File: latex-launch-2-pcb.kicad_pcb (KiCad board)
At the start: 4 copper layers, 9 parts, among them J1 Conn_RockBLOCK, J2 Switch_RockBLOCK, J3 Conn_FeatherWeight, J4 Conn_LightAPRS, J5 Conn_MicroSD

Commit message: idk
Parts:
- added H1: MountingHole, MountingHole:MountingHole_3.2mm_M3_DIN965_Pad, F.Cu at (114.6, 73.9)
- added H2: MountingHole, MountingHole:MountingHole_3.2mm_M3_DIN965_Pad, F.Cu at (114.6, 129.5)
- added H3: MountingHole, MountingHole:MountingHole_3.2mm_M3_DIN965_Pad, F.Cu at (186.7, 129.5)
- added H4: MountingHole, MountingHole:MountingHole_3.2mm_M3_DIN965_Pad, F.Cu at (186.7, 73.9)
- added J6: Conn_GY-512_MPU6050, Module:GY-521 MPU6050, F.Cu at (152.7, 91.4)
- moved J2 112.7 mm to (183.9, 122.7), turned to 180 degrees
- moved J1 111.1 mm to (186.6, 109.8), turned to 90 degrees
- moved J3 107.7 mm to (186.3, 86.9), turned to 90 degrees
- moved R2 100.7 mm to (169.2, 106.2), turned to 90 degrees
- moved R1 94.2 mm to (174.2, 96.0), turned to -90 degrees
- moved A1 83.6 mm to (133.6, 129.4), turned to 90 degrees
- moved J4 70.6 mm to (117.2, 115.3)
- moved C1 43.4 mm to (148.8, 105.7), turned to 180 degrees
- moved J5 5.93 mm to (123.7, 91.2), turned to 90 degrees
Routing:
- net +BATT: track 0.00 -> 96.5 mm, vias 0 -> 2
- net /I2C_SDA: track 0.00 -> 90.7 mm, vias 0 -> 3
- net /I2C_SCL: track 0.00 -> 82.8 mm, vias 0 -> 3
- net +3V3: track 0.00 -> 73.4 mm, vias 0 -> 2
- net /CS_SDCard: track 0.00 -> 68.3 mm, vias 0 -> 2
- net /SPI_MISO: track 0.00 -> 60.3 mm, vias 0 -> 1
- net /SPI_MOSI: track 0.00 -> 59.3 mm, vias 0 -> 3
- net /SPI_SCK: track 0.00 -> 53.7 mm, vias 0 -> 1
- net /Tx: track 0.00 -> 21.1 mm
- net /Rx: track 0.00 -> 21.1 mm
- net /Tx_RockBLOCK: track 0.00 -> 15.3 mm
- net /Rx_RockBLOCK: track 0.00 -> 8.97 mm
- added copper zone on F.Cu, net GND
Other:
- board outline added: 82.6 x 66.3 mm

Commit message: better pcb
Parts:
- moved H4 118.2 mm to (68.6, 68.6)
- moved J3 117.8 mm to (70.6, 108.7), turned to -90 degrees
- moved J1 106.5 mm to (81.8, 128.2)
- moved J2 98.2 mm to (87.1, 105.9), turned to 0 degrees
- moved H3 80.2 mm to (134.6, 68.6)
- moved R1 79.5 mm to (95.5, 85.1), turned to 0 degrees
- moved H1 76.3 mm to (68.3, 134.6)
- moved R2 69.0 mm to (105.7, 79.2), turned to 180 degrees
- moved A1 52.1 mm to (110.9, 82.5), turned to 0 degrees
- moved J6 52.1 mm to (101.6, 101.6), turned to 0 degrees
- moved C1 49.0 mm to (101.1, 116.8), turned to 0 degrees
- moved J4 47.4 mm to (70.5, 123.4)
- moved J5 46.6 mm to (77.2, 88.6)
- moved H2 20.7 mm to (134.6, 134.6)
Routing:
- net +3V3: track 73.4 -> 39.8 mm, vias 2 -> 0
- net /I2C_SCL: track 82.8 -> 111.7 mm, vias 3 -> 1
- net /SPI_MISO: track 60.3 -> 34.1 mm, vias 1 -> 0
- net /SPI_MOSI: track 59.3 -> 34.3 mm, vias 3 -> 0
- net /I2C_SDA: track 90.7 -> 105.4 mm, vias 3 -> 1
- net +BATT: track 96.5 -> 109.7 mm, vias 2 -> 0
- net /SPI_SCK: track 53.7 -> 42.0 mm, vias 1 -> 0
- net /CS_SDCard: track 68.3 -> 57.3 mm, vias 2 -> 0
- net /Rx_RockBLOCK: track 8.97 -> 19.4 mm
- net /Tx: track 21.1 -> 30.5 mm
- net /Rx: track 21.1 -> 26.7 mm
- net /Tx_RockBLOCK: track 15.3 -> 12.3 mm
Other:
- board size 82.6 x 66.3 mm -> 76.2 x 76.2 mm

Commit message: PCB version 2
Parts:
- removed H1, H2, H3, H4: MountingHole, MountingHole:MountingHole_3.2mm_M3_DIN965_Pad
- added J7: Conn_MicroSD, Latex Launch 2 Footprints:Adafruit_MicroSD_Breakout, F.Cu at (228.6, 113.0)
- added J8: Conn_HTU21DF, Latex Launch 2 Footprints:Adafruit_HTU21DF_Breakout, F.Cu at (174.1, 117.5)
- added R3: R_shunt, Connector_PinHeader_2.54mm:PinHeader_1x02_P2.54mm_Vertical, F.Cu at (201.9, 67.3)
- added R4: R_shunt, Connector_PinHeader_2.54mm:PinHeader_1x02_P2.54mm_Vertical, F.Cu at (207.3, 67.3)
- added U1: ~, Latex Launch 2 Footprints:Adafruit_RFM96W_LoRa_Breakout, F.Cu at (200.6, 110.7)
- A1: value Adafruit_Feather_M0_RFM9x_LoRa_Radio -> Adafruit_Feather_M0_Express; footprint Module:Adafruit_Feather_M0_RFM -> Module:Adafruit_Feather_M0_RFM_WithMountingHoles
- C1: value C0.1u -> C; footprint Capacitor_THT:C_Rect_L7.0mm_W2.5mm_P5.00mm -> Capacitor_THT:C_Rect_L4.6mm_W2.0mm_P2.50mm_MKS02_FKP02
- J1: value Conn_RockBLOCK -> Conn_GPS; footprint Connector_Molex:Molex_PicoBlade_53047-1010_1x10_P1.25mm_Vertical -> Latex Launch 2 Footprints:Adafruit_GPS_Breakout
- J2: value Switch_RockBLOCK -> Conn_LightAPRS-W_2.0; footprint Connector_PinSocket_2.54mm:PinSocket_2x03_P2.54mm_Vertical -> Connector_JST:JST_PH_S4B-PH-SM4-TB_1x04-1MP_P2.00mm_Horizontal
- J4: value Conn_LightAPRS -> Conn_RockBLOCK; footprint Connector_JST:JST_PH_S4B-PH-SM4-TB_1x04-1MP_P2.00mm_Horizontal -> Connector_Molex:Molex_PicoBlade_53047-1010_1x10_P1.25mm_Vertical
- J5: value Conn_MicroSD -> Conn_GY512_MPU6050; footprint Module:Adafruit_MicroSD_Breakout -> Latex Launch 2 Footprints:GY-521 MPU6050
- J6: value Conn_GY-512_MPU6050 -> Conn_BMP280; footprint Module:GY-521 MPU6050 -> Latex Launch 2 Footprints:Adafruit_BMP280_Breakout
- R1, R2: value R10k -> 10k
- moved J4 174.3 mm to (230.4, 54.0), turned to 90 degrees
- moved J1 150.7 mm to (224.8, 80.5), turned to 180 degrees
- moved J5 126.1 mm to (203.2, 82.5), turned to 0 degrees
- moved J3 104.7 mm to (172.2, 83.6)
- moved R1 96.1 mm to (190.5, 70.9), turned to 180 degrees
- moved J2 92.3 mm to (172.2, 70.1), turned to -90 degrees
- moved C1 88.2 mm to (168.7, 60.2)
- moved R2 86.1 mm to (190.5, 64.5)
- moved J6 75.0 mm to (176.5, 99.3), turned to 90 degrees
- moved A1 72.9 mm to (180.3, 60.6), turned to 90 degrees
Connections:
- A1 pad 14: /Rx -> Net-(A1-RX/D0)
- A1 pad 15: /Tx -> Net-(A1-TX/D1)
- A1 pad 19: /CS_SDCard -> /CS_SD
- A1 pad 20: unconnected-(A1-D6-Pad20) -> /EN_GPS
- A1 pad 21: unconnected-(A1-D9-Pad21) -> /EN_RockBLOCK
- A1 pad 22: unconnected-(A1-D10-Pad22) -> /CS_RFM96W
- A1 pad 23: unconnected-(A1-D11-Pad23) -> /CS_BMP280
- A1 pad 26: +BATT -> unconnected-(A1-USB-Pad26)
- A1 pad 28: unconnected-(A1-VBAT-Pad28) -> +BATT
- A1 pad 29: unconnected-(A1-ANT-Pad29) -> (no net)
- A1 pad 30: unconnected-(A1-DIO5-Pad30) -> (no net)
- A1 pad 31: unconnected-(A1-DIO3-Pad31) -> (no net)
- A1 pad 32: unconnected-(A1-DIO2-Pad32) -> (no net)
- J1 pad 1: /Rx_RockBLOCK -> unconnected-(J1-Pin_1-Pad1)
- J1 pad 2: unconnected-(J1-Pin_2-Pad2) -> /EN_GPS
- J1 pad 5: unconnected-(J1-Pin_5-Pad5) -> /Rx_iso
- J1 pad 6: /Tx_RockBLOCK -> /Tx_iso
- J1 pad 7: unconnected-(J1-Pin_7-Pad7) -> GND
- J1 pad 8: +BATT -> +3V3
- J2 pad 1: unconnected-(J2-Pin_1-Pad1) -> /I2C_SCL
- J2 pad 2: unconnected-(J2-Pin_2-Pad2) -> /I2C_SDA
- J2 pad 3: /Rx -> +BATT
- J2 pad 4: /Tx -> GND
- J3 pad 1: +BATT -> +3V3
- J4 pad 1: GND -> /Rx_iso
- J4 pad 2: +BATT -> unconnected-(J4-Pin_2-Pad2)
- J4 pad 3: /I2C_SCL -> unconnected-(J4-Pin_3-Pad3)
- J4 pad 4: /I2C_SDA -> unconnected-(J4-Pin_4-Pad4)
- J5 pad 3: /SPI_SCK -> /I2C_SCL
- J5 pad 4: /SPI_MISO -> /I2C_SDA
- J5 pad 5: /SPI_MOSI -> unconnected-(J5-Pin_5-Pad5)
- J5 pad 6: /CS_SDCard -> unconnected-(J5-Pin_6-Pad6)
- J6 pad 1: +BATT -> +3V3
- J6 pad 2: GND -> unconnected-(J6-Pin_2-Pad2)
- J6 pad 3: /I2C_SCL -> GND
- J6 pad 4: /I2C_SDA -> /SPI_SCK
- J6 pad 5: unconnected-(J6-Pin_5-Pad5) -> /SPI_MISO
- J6 pad 6: unconnected-(J6-Pin_6-Pad6) -> /SPI_MOSI
- J6 pad 7: unconnected-(J6-Pin_7-Pad7) -> /CS_BMP280
- R2 pad 1: /I2C_SCL -> +3V3
- R2 pad 2: +3V3 -> /I2C_SCL
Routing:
- net +3V3: track 39.8 -> 148.8 mm, vias 0 -> 1
- net /CS_SD: track 0.00 -> 78.9 mm
- net /CS_RFM96W: track 0.00 -> 64.7 mm
- net /CS_BMP280: track 0.00 -> 59.6 mm
- net /SPI_MOSI: track 34.3 -> 92.1 mm, vias 0 -> 2
- net /CS_SDCard: track 57.3 -> 0.00 mm
- net /SPI_MISO: track 34.1 -> 89.1 mm, vias 0 -> 2
- net /SPI_SCK: track 42.0 -> 94.0 mm
- net /EN_GPS: track 0.00 -> 42.9 mm
- net /Rx_iso: track 0.00 -> 38.6 mm
- net /Tx_iso: track 0.00 -> 37.1 mm
- net /Tx: track 30.5 -> 0.00 mm
- net /EN_RockBLOCK: track 0.00 -> 29.6 mm
- net /Rx: track 26.7 -> 0.00 mm
- net +BATT: track 109.7 -> 86.6 mm
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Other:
- board size 76.2 x 76.2 mm -> 76.2 x 88.9 mm

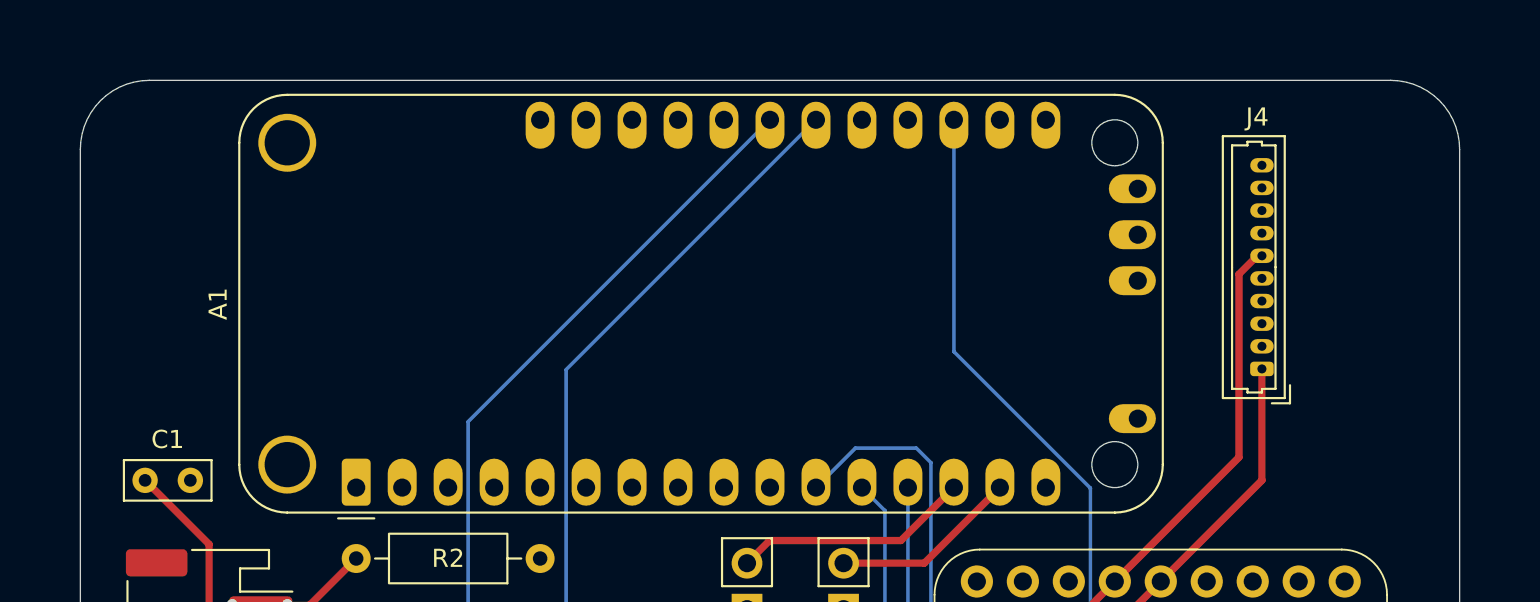
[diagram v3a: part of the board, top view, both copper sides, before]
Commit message: PCB v2 added mounting holes
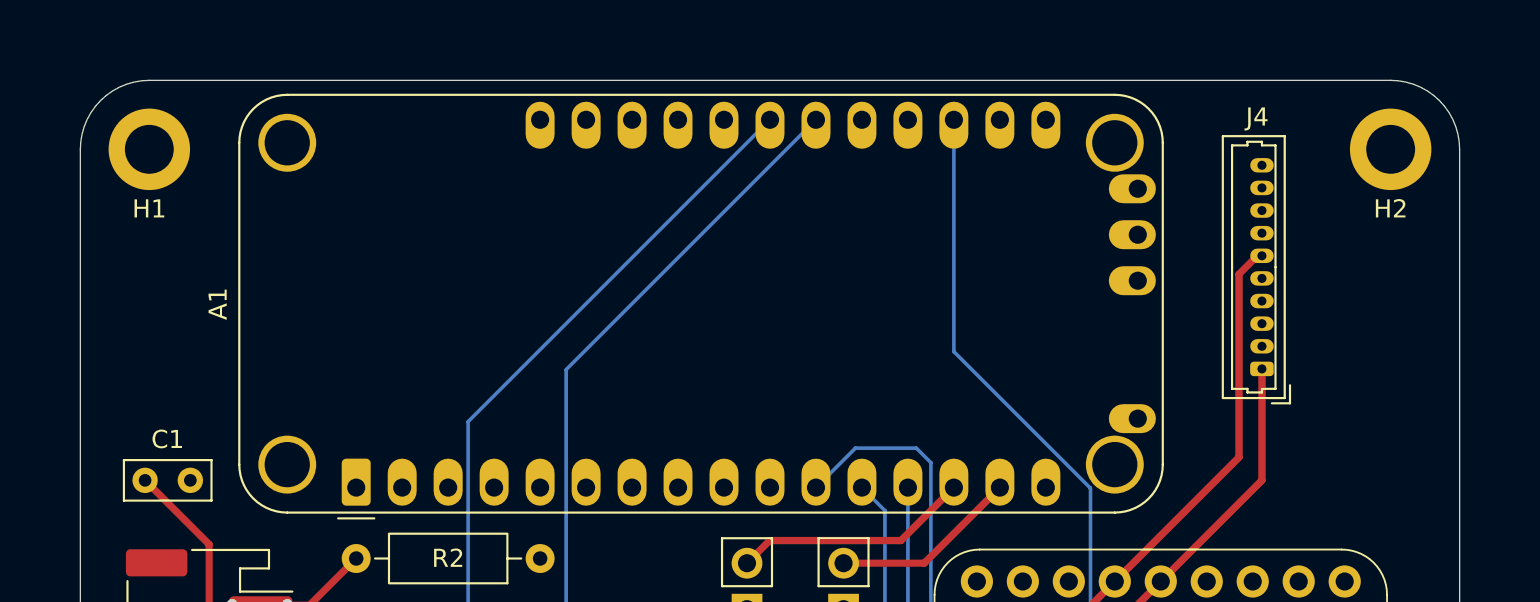
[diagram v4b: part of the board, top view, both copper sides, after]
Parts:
- added H1: MountingHole, MountingHole:MountingHole_2.7mm_M2.5_ISO7380_Pad, F.Cu at (168.9, 41.9)
- added H2: MountingHole, MountingHole:MountingHole_2.7mm_M2.5_ISO7380_Pad, F.Cu at (237.5, 41.9)
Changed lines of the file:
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@@
 		)
+	)
+	(footprint "MountingHole:MountingHole_2.7mm_M2.5_ISO7380_Pad"
+		(layer "F.Cu")
+		(at 168.91 41.91)
+		(descr "Mounting Hole 2.7mm, M2.5, generated by kicad-footprint-generator mountinghole.py")
+		(tags "mountinghole M2.5 ISO7380")
+		(property "Reference" "H1"
+			(at 0 3.302 0)
+			(layer "F.SilkS")
+			(effects
+				(font
+					(size 1 1)
+					(thickness 0.15)
+				)
+			)
+		)
+		(property "Value" "MountingHole"
+			(at 3.302 2.032 90)
+			(layer "F.Fab")
+			(effects
+				(font
+					(size 1 1)
+					(thickness 0.15)
+				)
+			)
+		)
+		(property "Datasheet" "~"
+			(at 0 0 0)
+			(layer "F.Fab")
+			(hide yes)
+			(effects
+				(font
+					(size 1.27 1.27)
+					(thickness 0.15)
+				)
+			)
+		)
+		(property "Description" "Mounting Hole without connection"
+			(at 0 0 0)
+			(layer "F.Fab")
+			(hide yes)
+			(effects
+				(font
+					(size 1.27 1.27)
+					(thickness 0.15)
+				)
+			)
+		)
+		(property ki_fp_filters "MountingHole*")
+		(sheetname "/")
+		(sheetfile "latex-launch-2-pcb.kicad_sch")
+		(attr exclude_from_pos_files exclude_from_bom)
+		(fp_circle
+			(center 0 0)
+			(end 2.25 0)
+			(stroke
+				(width 0.15)
+				(type solid)
+			)
+			(fill no)
+			(layer "Cmts.User")
+		)
+		(fp_circle
+			(center 0 0)
+			(end 2.5 0)
+			(stroke
+				(width 0.05)
+				(type solid)
+			)
+			(fill no)
+			(layer "F.CrtYd")
+		)
+		(fp_text user "${REFERENCE}"
+			(at 0 0 0)
+			(layer "F.Fab")
+			(effects
+				(font
+					(size 1 1)
+					(thickness 0.15)
+				)
+			)
+		)
+		(pad "1" thru_hole circle
+			(at 0 0)
+			(size 4.5 4.5)
+			(drill 2.7)
+			(layers "*.Cu" "*.Mask")
+			(remove_unused_layers no)
+			(zone_connect 2)
+		)
+		(embedded_fonts no)
 	)
 	(footprint "Capacitor_THT:C_Rect_L4.6mm_W2.0mm_P2.50mm_MKS02_FKP02"
@@
 			)
 		)
-		(pad "" np_thru_hole circle
+		(pad "" thru_hole circle
 			(at 1.27 -3.81)
 			(size 3.2 3.2)
 			(drill 2.5)
 			(layers "*.Cu" "*.Mask")
-		)
-		(pad "" np_thru_hole circle
+			(remove_unused_layers no)
+		)
+		(pad "" thru_hole circle
 			(at 1.27 41.91)
-			(size 2.54 2.54)
-			(drill 2.54)
-			(layers "*.Cu" "*.Mask")
-		)
-		(pad "" np_thru_hole circle
+			(size 3.2 3.2)
+			(drill 2.5)
+			(layers "*.Cu" "*.Mask")
+			(remove_unused_layers no)
+		)
+		(pad "" thru_hole circle
 			(at 19.05 -3.81)
 			(size 3.2 3.2)
 			(drill 2.5)
 			(layers "*.Cu" "*.Mask")
-		)
-		(pad "" np_thru_hole circle
+			(remove_unused_layers no)
+		)
+		(pad "" thru_hole circle
 			(at 19.05 41.91)
-			(size 2.54 2.54)
-			(drill 2.54)
-			(layers "*.Cu" "*.Mask")
+			(size 3.2 3.2)
+			(drill 2.5)
+			(layers "*.Cu" "*.Mask")
+			(remove_unused_layers no)
 		)
 		(pad "1" thru_hole roundrect
@@
 		)
 		(embedded_fonts no)
+	)
+	(footprint "MountingHole:MountingHole_2.7mm_M2.5_ISO7380_Pad"
+		(layer "F.Cu")
+		(at 237.49 41.91)
+		(descr "Mounting Hole 2.7mm, M2.5, generated by kicad-footprint-generator mountinghole.py")
+		(tags "mountinghole M2.5 ISO7380")
+		(property "Reference" "H2"
+			(at 0 3.302 0)
+			(layer "F.SilkS")
+			(effects
+				(font
+					(size 1 1)
+					(thickness 0.15)
+				)
+			)
+		)
+		(property "Value" "MountingHole"
+			(at -3.556 2.032 90)
+			(layer "F.Fab")
+			(effects
+				(font
+					(size 1 1)
+					(thickness 0.15)
+				)
+			)
+		)
+		(property "Datasheet" "~"
+			(at 0 0 0)
+			(layer "F.Fab")
+			(hide yes)
+			(effects
+				(font
+					(size 1.27 1.27)
+					(thickness 0.15)
+				)
+			)
+		)
+		(property "Description" "Mounting Hole without connection"
+			(at 0 0 0)
+			(layer "F.Fab")
+			(hide yes)
+			(effects
+				(font
+					(size 1.27 1.27)
+					(thickness 0.15)
+				)
+			)
+		)
+		(property ki_fp_filters "MountingHole*")
+		(sheetname "/")
+		(sheetfile "latex-launch-2-pcb.kicad_sch")
+		(attr exclude_from_pos_files exclude_from_bom)
+		(fp_circle
+			(center 0 0)
+			(end 2.25 0)
+			(stroke
+				(width 0.15)
+				(type solid)
+			)
+			(fill no)
+			(layer "Cmts.User")
+		)
+		(fp_circle
+			(center 0 0)
+			(end 2.5 0)
+			(stroke
+				(width 0.05)
+				(type solid)
+			)
+			(fill no)
+			(layer "F.CrtYd")
+		)
+		(fp_text user "${REFERENCE}"
+			(at 0 0 0)
+			(layer "F.Fab")
+			(effects
+				(font
+					(size 1 1)
+					(thickness 0.15)
+				)
+			)
+		)
+		(pad "1" thru_hole circle
+			(at 0 0)
+			(size 4.5 4.5)
+			(drill 2.7)
+			(layers "*.Cu" "*.Mask")
+			(remove_unused_layers no)
+			(zone_connect 2)
+		)
+		(embedded_fonts no)

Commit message: updated a lot
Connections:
- A1 pad 26: unconnected-(A1-USB-Pad26) -> +BATT
- A1 pad 28: +BATT -> unconnected-(A1-VBAT-Pad28)
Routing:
- net /I2C_SCL: vias 2 -> 1
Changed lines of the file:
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@@
 	(net 1 "unconnected-(A1-A3-Pad8)")
 	(net 2 "unconnected-(A1-D12-Pad24)")
-	(net 3 "unconnected-(A1-USB-Pad26)")
+	(net 3 "unconnected-(A1-VBAT-Pad28)")
 	(net 4 "+3V3")
 	(net 5 "Net-(A1-RX{slash}D0)")
@@
 			(layers "*.Cu" "*.Mask")
 			(remove_unused_layers no)
-			(net 3 "unconnected-(A1-USB-Pad26)")
+			(net 23 "+BATT")
 			(pinfunction "USB")
 			(pintype "power_in")
@@
 			(layers "*.Cu" "*.Mask")
 			(remove_unused_layers no)
-			(net 23 "+BATT")
+			(net 3 "unconnected-(A1-VBAT-Pad28)")
 			(pinfunction "VBAT")
 			(pintype "power_in")
@@
 	)
 	(segment
-		(start 190.5 40.2785)
-		(end 188.5955 40.2785)
+		(start 200.4035 45.2895)
+		(end 195.58 40.466)
+		(width 0.4)
+		(layer "In1.Cu")
+		(net 23)
+	)
+	(segment
+		(start 230.3755 45.2895)
+		(end 200.4035 45.2895)
+		(width 0.4)
+		(layer "In1.Cu")
+		(net 23)
+	)
+	(segment
+		(start 183.662 45.212)
+		(end 191.008 45.212)
 		(width 0.4)
 		(layer "In1.Cu")
@@
 	(segment
 		(start 230.378 45.292)
-		(end 195.5135 45.292)
+		(end 230.3755 45.2895)
 		(width 0.4)
 		(layer "In1.Cu")
@@
 	)
 	(segment
-		(start 195.5135 45.292)
-		(end 190.5 40.2785)
+		(start 195.58 40.64)
+		(end 195.58 40.2785)
 		(width 0.4)
 		(layer "In1.Cu")
@@
 	)
 	(segment
-		(start 188.5955 40.2785)
-		(end 168.676 60.198)
+		(start 195.58 40.466)
+		(end 195.58 40.2785)
+		(width 0.4)
+		(layer "In1.Cu")
+		(net 23)
+	)
+	(segment
+		(start 191.008 45.212)
+		(end 195.58 40.64)
+		(width 0.4)
+		(layer "In1.Cu")
+		(net 23)
+	)
+	(segment
+		(start 168.676 60.198)
+		(end 183.662 45.212)
 		(width 0.4)
 		(layer "In1.Cu")
@@
 		(size 0.6)
 		(drill 0.3)
-		(layers "F.Cu" "B.Cu")
-		(net 25)
-	)
-	(via
-		(at 176.53 67.056)
-		(size 0.6)
-		(drill 0.3)
